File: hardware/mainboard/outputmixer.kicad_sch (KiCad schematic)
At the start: 14 parts, among them J117 Mix, U12 TL074, U6 TL074

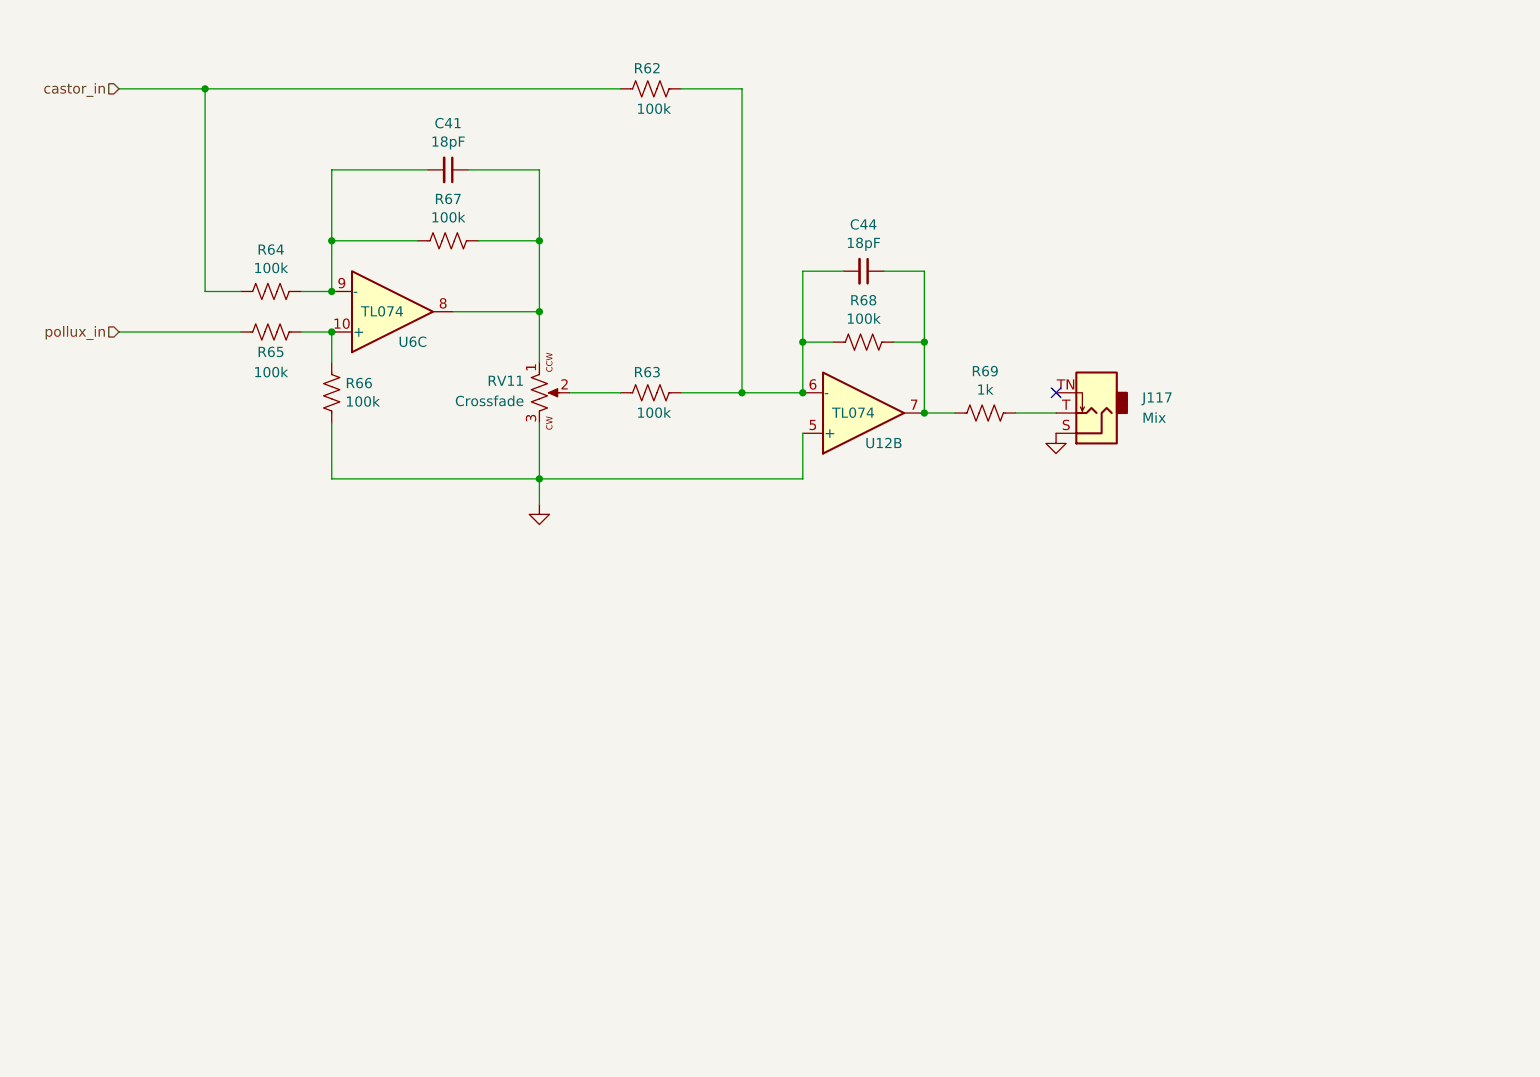
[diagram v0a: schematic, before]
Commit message: Progress on cleaning up the schematics
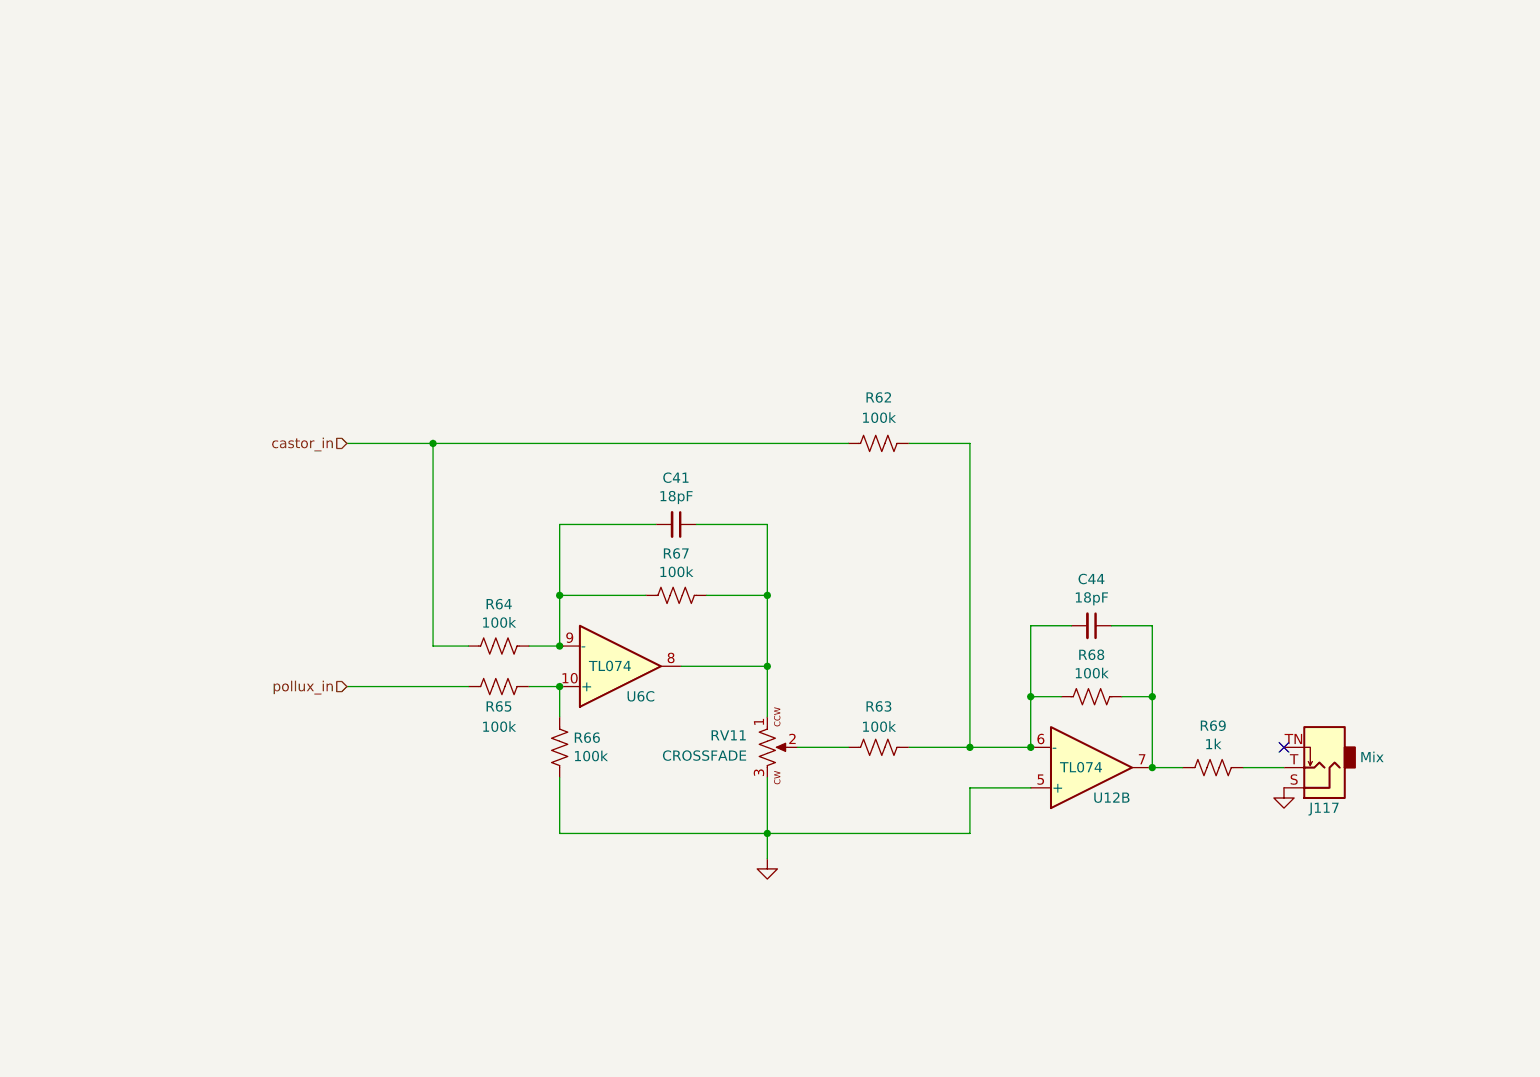
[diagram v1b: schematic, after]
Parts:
- RV11: value Crossfade -> CROSSFADE
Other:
- moved on the sheet: C41, C44, J117, R62, R63, R64, R65, R66, R67, R68, R69, RV11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

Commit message: Cleanup MCU schematic
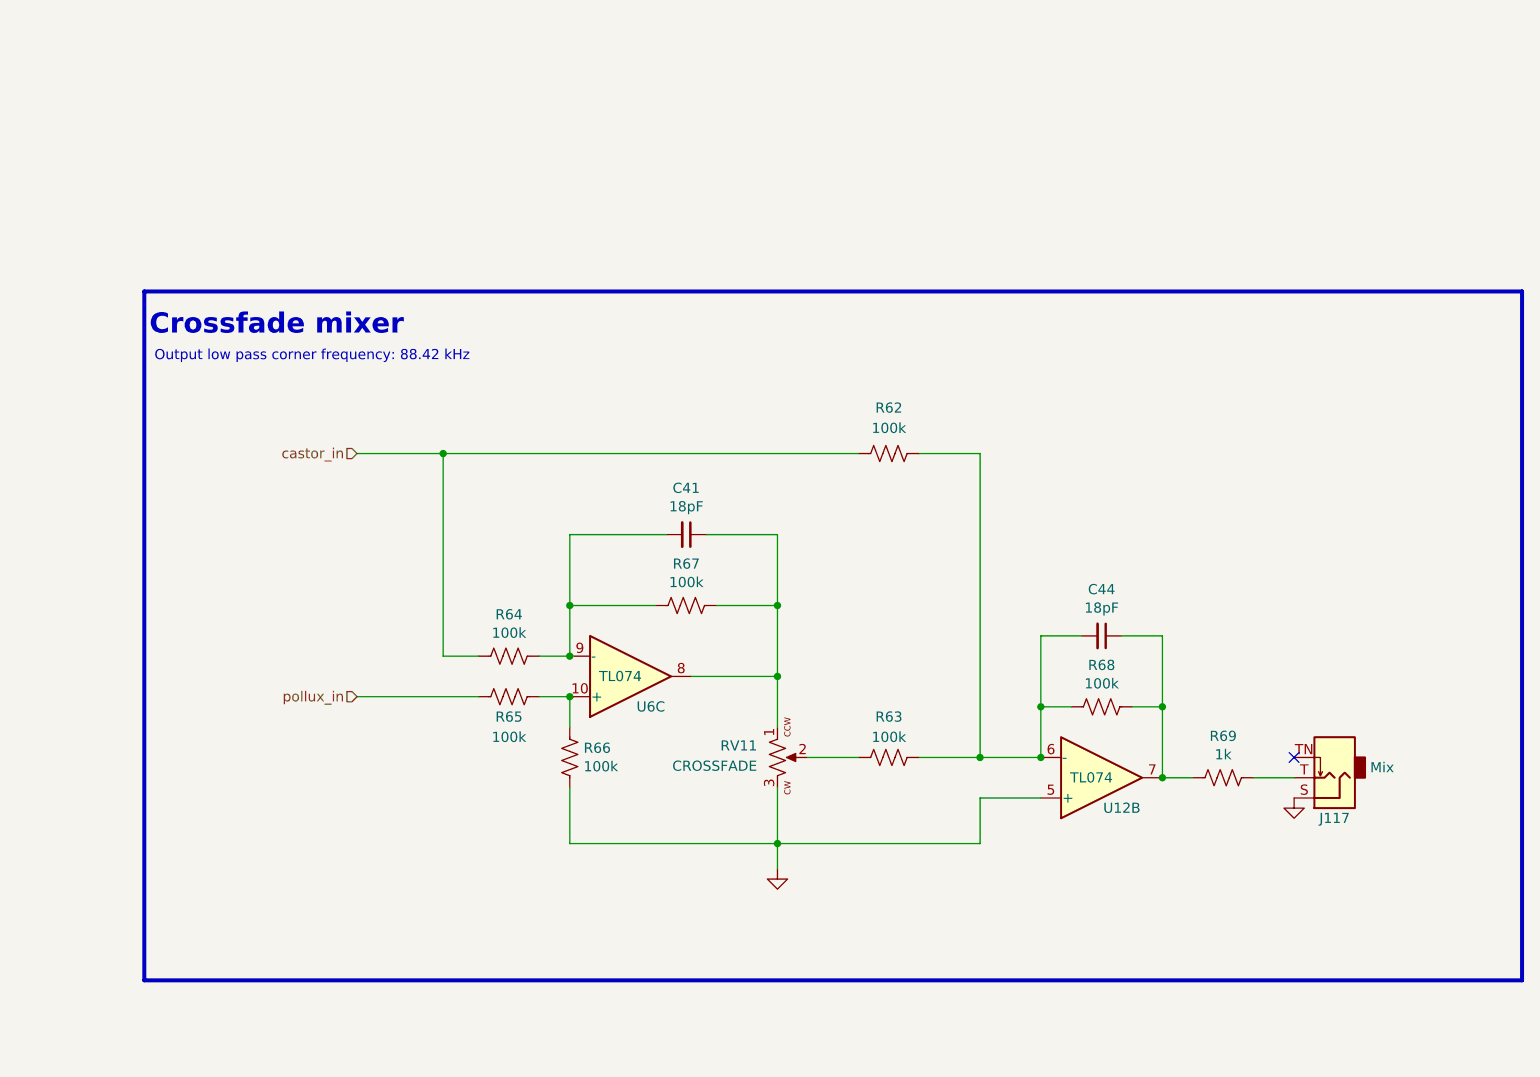
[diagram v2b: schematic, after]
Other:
- note added: "Crossfade mixer"
- note added: "Output low pass corner frequency: 88.42 kHz"
- moved on the sheet: C41, C44, J117, R62, R63, R64, R65, R66, R67, R68, R69, RV11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

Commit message: More schematic cleanup - nearly done!
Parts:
- added J1: EXT, Connector_JST:JST_GH_BM08B-GHS-TBT_1x08-1MP_P1.25mm_Vertical, symbol Connector_Generic:Conn_01x08
- J117: value Mix -> MIX
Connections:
- net GND: now also J1.1 (Pin_1), J1.8 (Pin_8)
- net castor_in renamed CASTOR_MIX_IN
- net pollux_in renamed POLLUX_MIX_IN
- new net CASTOR_PULSE_IN: J1.6 (Pin_6)
- new net CASTOR_RAMP_IN: J1.7 (Pin_7)
- new net CASTOR_SUB_IN: J1.5 (Pin_5)
- new net POLLUX_PULSE_IN: J1.3 (Pin_3)
- new net POLLUX_RAMP_IN: J1.2 (Pin_2)
- new net POLLUX_SUB_IN: J1.4 (Pin_4)
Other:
- moved on the sheet: C41, C44, J117, R62, R63, R64, R65, R66, R67, R68, R69, RV11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
